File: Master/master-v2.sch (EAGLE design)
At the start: 59 parts, among them J1 ISP, K1 653002114822, K2 653002114822, K3 653002114822, K4 653002114822, U1 ATMEGA128RFA1, U3 ULN2003ANE4, Y1 16MHz, Y2 32.768kHz

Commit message: changes to master-v2
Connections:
- removed net N$21: U$3.SDA
- removed net N$22: U$6.SCL
- removed net N$23: U$6.SDA
- removed net VDD: C12.+, U$2.VO
- net 3.3V: now also C12.+, U$2.VO
- net SCL: now also U$6.SCL
- net SDA: now also U$3.SDA, U$6.SDA
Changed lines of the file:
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@@
 <label x="-5.08" y="99.06" size="1.27" layer="95" rot="MR0" xref="yes"/>
+</segment>
+<segment>
+<pinref part="U$3" gate="G$1" pin="SDA"/>
+<wire x1="-213.36" y1="78.74" x2="-210.82" y2="78.74" width="0.1524" layer="91"/>
+<wire x1="-210.82" y1="78.74" x2="-210.82" y2="81.28" width="0.1524" layer="91"/>
+<wire x1="-210.82" y1="81.28" x2="-208.28" y2="81.28" width="0.1524" layer="91"/>
+<label x="-208.28" y="81.28" size="1.778" layer="95" xref="yes"/>
+</segment>
+<segment>
+<pinref part="U$6" gate="G$1" pin="SDA"/>
+<wire x1="-111.76" y1="78.74" x2="-109.22" y2="78.74" width="0.1524" layer="91"/>
+<wire x1="-109.22" y1="78.74" x2="-109.22" y2="81.28" width="0.1524" layer="91"/>
+<wire x1="-109.22" y1="81.28" x2="-106.68" y2="81.28" width="0.1524" layer="91"/>
+<label x="-106.68" y="81.28" size="1.778" layer="95" xref="yes"/>
 </segment>
 </net>
@@
 <wire x1="-213.36" y1="81.28" x2="-213.36" y2="86.36" width="0.1524" layer="91"/>
 <wire x1="-213.36" y1="86.36" x2="-210.82" y2="86.36" width="0.1524" layer="91"/>
-<label x="-208.28" y="86.36" size="1.778" layer="95"/>
+<label x="-210.82" y="86.36" size="1.778" layer="95" xref="yes"/>
+</segment>
+<segment>
+<pinref part="U$6" gate="G$1" pin="SCL"/>
+<wire x1="-111.76" y1="81.28" x2="-111.76" y2="86.36" width="0.1524" layer="91"/>
+<wire x1="-111.76" y1="86.36" x2="-106.68" y2="86.36" width="0.1524" layer="91"/>
+<label x="-106.68" y="86.36" size="1.778" layer="95" xref="yes"/>
 </segment>
 </net>
@@
 <pinref part="U3" gate="A" pin="4B"/>
 <wire x1="-78.74" y1="226.06" x2="-81.28" y2="226.06" width="0.1524" layer="91"/>
-<label x="-86.36" y="226.06" size="1.778" layer="95"/>
+<label x="-81.28" y="226.06" size="1.778" layer="95" rot="R180" xref="yes"/>
 </segment>
 </net>
@@
 <pinref part="U3" gate="A" pin="3B"/>
 <wire x1="-78.74" y1="228.6" x2="-81.28" y2="228.6" width="0.1524" layer="91"/>
-<label x="-86.36" y="228.6" size="1.778" layer="95"/>
+<label x="-81.28" y="228.6" size="1.778" layer="95" rot="R180" xref="yes"/>
 </segment>
 </net>
@@
 <pinref part="U3" gate="A" pin="2B"/>
 <wire x1="-78.74" y1="231.14" x2="-81.28" y2="231.14" width="0.1524" layer="91"/>
-<label x="-86.36" y="231.14" size="1.778" layer="95"/>
+<label x="-81.28" y="231.14" size="1.778" layer="95" rot="R180" xref="yes"/>
 </segment>
 </net>
@@
 <pinref part="U3" gate="A" pin="1B"/>
 <wire x1="-78.74" y1="233.68" x2="-81.28" y2="233.68" width="0.1524" layer="91"/>
-<label x="-86.36" y="233.68" size="1.778" layer="95"/>
+<label x="-81.28" y="233.68" size="1.778" layer="95" rot="R180" xref="yes"/>
 </segment>
 </net>
@@
 <wire x1="-99.06" y1="76.2" x2="-88.9" y2="76.2" width="0.1524" layer="91"/>
 <junction x="-88.9" y="76.2"/>
+</segment>
+<segment>
+<pinref part="U$2" gate="G$1" pin="VO"/>
+<wire x1="-121.92" y1="172.72" x2="-119.38" y2="172.72" width="0.1524" layer="91"/>
+<pinref part="C12" gate="G$1" pin="+"/>
+<wire x1="-119.38" y1="172.72" x2="-116.84" y2="172.72" width="0.1524" layer="91"/>
+<wire x1="-119.38" y1="167.64" x2="-119.38" y2="172.72" width="0.1524" layer="91"/>
+<junction x="-119.38" y="172.72"/>
+<label x="-116.84" y="172.72" size="1.778" layer="95" xref="yes"/>
 </segment>
 </net>
@@
 </segment>
 </net>
-<net name="VDD" class="0">
-<segment>
-<pinref part="U$2" gate="G$1" pin="VO"/>
-<wire x1="-121.92" y1="172.72" x2="-119.38" y2="172.72" width="0.1524" layer="91"/>
-<label x="-116.84" y="175.26" size="1.778" layer="95"/>
-<pinref part="C12" gate="G$1" pin="+"/>
-<wire x1="-119.38" y1="172.72" x2="-116.84" y2="172.72" width="0.1524" layer="91"/>
-<wire x1="-119.38" y1="167.64" x2="-119.38" y2="172.72" width="0.1524" layer="91"/>
-<junction x="-119.38" y="172.72"/>
-</segment>
-</net>
 <net name="N$1" class="0">
 <segment>
@@
 </segment>
 </net>
-<net name="N$21" class="0">
-<segment>
-<pinref part="U$3" gate="G$1" pin="SDA"/>
-<wire x1="-213.36" y1="78.74" x2="-210.82" y2="78.74" width="0.1524" layer="91"/>
-<wire x1="-210.82" y1="78.74" x2="-210.82" y2="83.82" width="0.1524" layer="91"/>
-<label x="-208.28" y="81.28" size="1.778" layer="95"/>
-</segment>
-</net>
-<net name="N$22" class="0">
-<segment>
-<pinref part="U$6" gate="G$1" pin="SCL"/>
-<wire x1="-111.76" y1="81.28" x2="-111.76" y2="86.36" width="0.1524" layer="91"/>
-<wire x1="-111.76" y1="86.36" x2="-106.68" y2="86.36" width="0.1524" layer="91"/>
-</segment>
-</net>
-<net name="N$23" class="0">
-<segment>
-<pinref part="U$6" gate="G$1" pin="SDA"/>
-<wire x1="-111.76" y1="78.74" x2="-109.22" y2="78.74" width="0.1524" layer="91"/>
-<wire x1="-109.22" y1="78.74" x2="-109.22" y2="83.82" width="0.1524" layer="91"/>
-<wire x1="-109.22" y1="83.82" x2="-106.68" y2="83.82" width="0.1524" layer="91"/>
-</segment>
-</net>

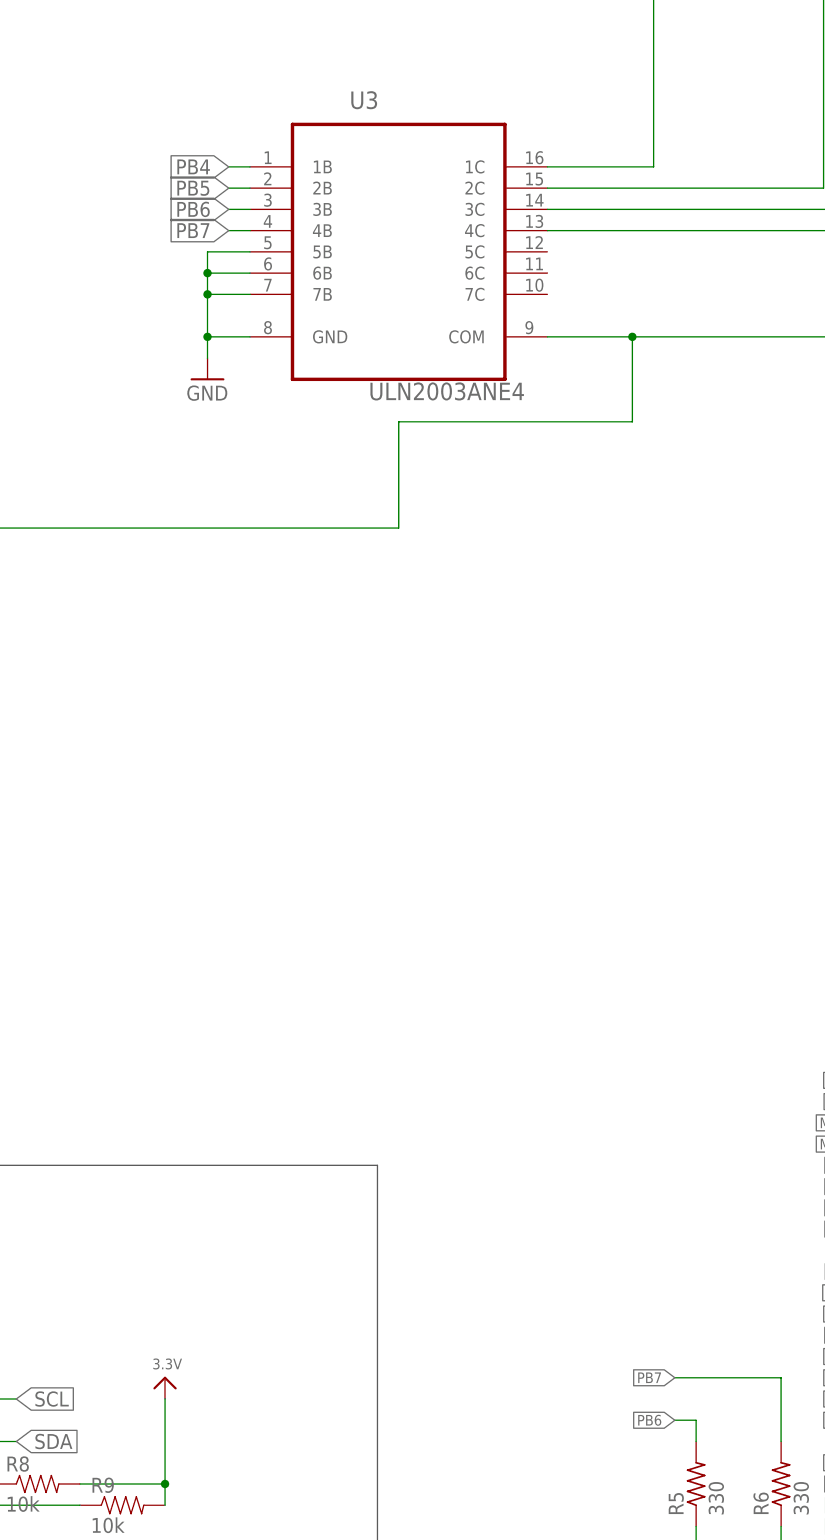
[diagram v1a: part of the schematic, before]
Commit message: Change motor pins in master v2
Changed Pin enumeration for motors. There was one conflict with one Led
so it was changed to another pin. Also routing of those pins was done.
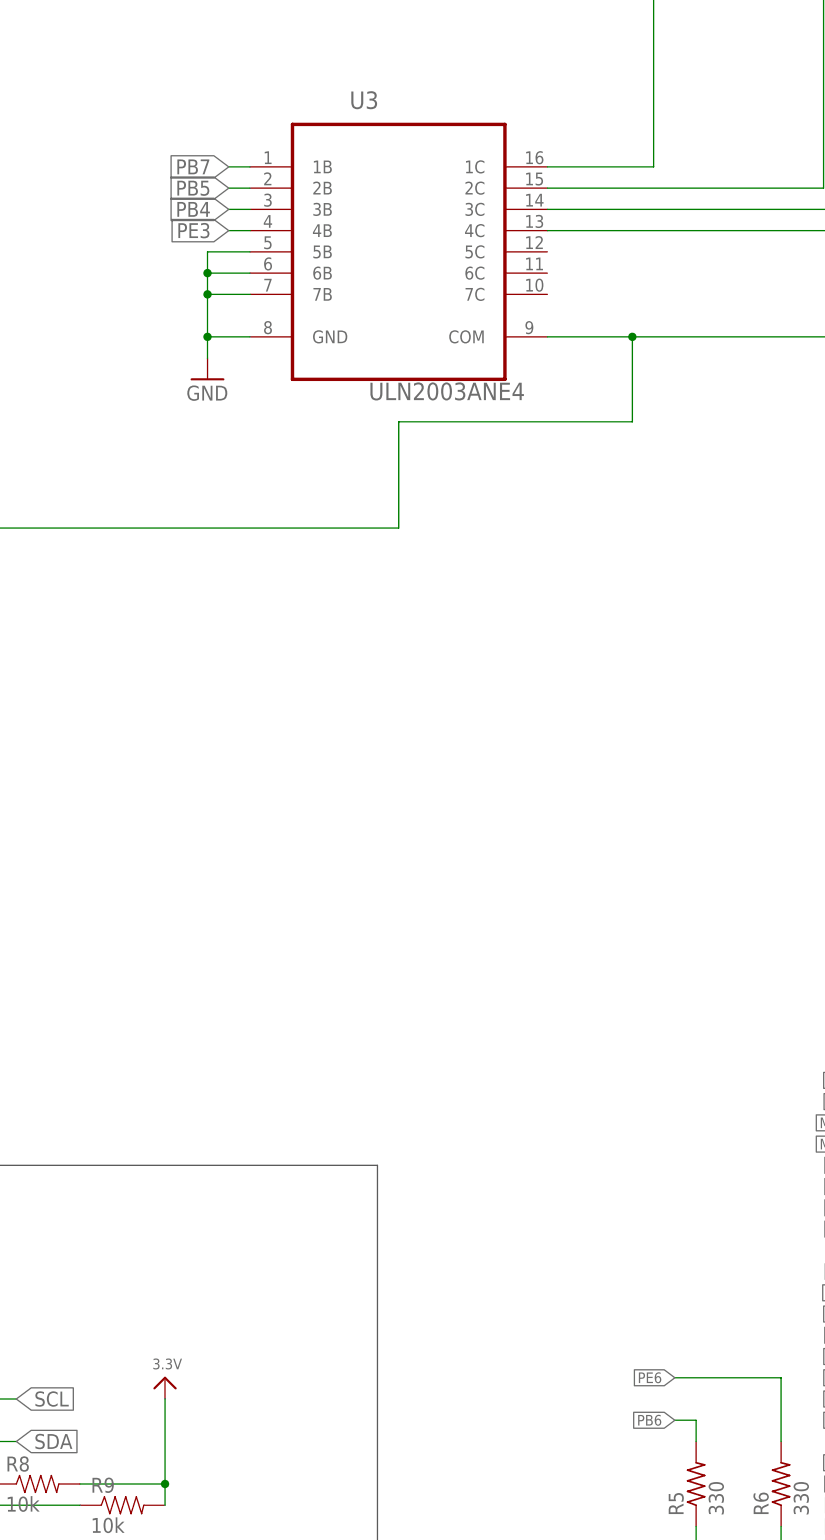
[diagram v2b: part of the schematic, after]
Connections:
- net PB4: now also U3.3B; no longer U3.1B
- net PB6: no longer U3.3B
- net PB7: now also U3.1B; no longer R6.2, U3.4B
- net PE3: now also U3.4B
- net PE6: now also R6.2
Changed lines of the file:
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@@
 <classes>
 <class number="0" name="default" width="0" drill="0">
+<clearance class="0" value="0.205"/>
 </class>
 <class number="1" name="RFSIG" width="0.4572" drill="0">
+<clearance class="0" value="0.205"/>
+<clearance class="1" value="0.205"/>
 </class>
 </classes>
@@
 <label x="-5.08" y="63.5" size="1.27" layer="95" rot="MR0" xref="yes"/>
 </segment>
+<segment>
+<pinref part="R6" gate="G$1" pin="2"/>
+<wire x1="-15.24" y1="81.28" x2="-15.24" y2="88.9" width="0.1524" layer="91"/>
+<wire x1="-15.24" y1="88.9" x2="-27.94" y2="88.9" width="0.1524" layer="91"/>
+<label x="-27.94" y="88.9" size="1.27" layer="95" rot="R180" xref="yes"/>
+</segment>
 </net>
 <net name="PE5" class="0">
@@
 <wire x1="-2.54" y1="71.12" x2="-5.08" y2="71.12" width="0.1524" layer="91"/>
 <label x="-5.08" y="71.12" size="1.27" layer="95" rot="MR0" xref="yes"/>
+</segment>
+<segment>
+<pinref part="U3" gate="A" pin="4B"/>
+<wire x1="-78.74" y1="226.06" x2="-81.28" y2="226.06" width="0.1524" layer="91"/>
+<label x="-81.28" y="226.06" size="1.778" layer="95" rot="R180" xref="yes"/>
 </segment>
 </net>
@@
 </segment>
 <segment>
-<pinref part="R6" gate="G$1" pin="2"/>
-<wire x1="-15.24" y1="81.28" x2="-15.24" y2="88.9" width="0.1524" layer="91"/>
-<wire x1="-15.24" y1="88.9" x2="-27.94" y2="88.9" width="0.1524" layer="91"/>
-<label x="-27.94" y="88.9" size="1.27" layer="95" rot="R180" xref="yes"/>
-</segment>
-<segment>
-<pinref part="U3" gate="A" pin="4B"/>
-<wire x1="-78.74" y1="226.06" x2="-81.28" y2="226.06" width="0.1524" layer="91"/>
-<label x="-81.28" y="226.06" size="1.778" layer="95" rot="R180" xref="yes"/>
+<pinref part="U3" gate="A" pin="1B"/>
+<wire x1="-78.74" y1="233.68" x2="-81.28" y2="233.68" width="0.1524" layer="91"/>
+<label x="-81.28" y="233.68" size="1.778" layer="95" rot="R180" xref="yes"/>
 </segment>
 </net>
@@
 <label x="-27.94" y="83.82" size="1.27" layer="95" rot="R180" xref="yes"/>
 </segment>
+</net>
+<net name="PB5" class="0">
+<segment>
+<pinref part="U1" gate="G$1" pin="PB5(OC1A/PCINT5)"/>
+<label x="-5.08" y="111.76" size="1.27" layer="95" rot="MR0" xref="yes"/>
+<wire x1="-2.54" y1="111.76" x2="-5.08" y2="111.76" width="0.1524" layer="91"/>
+</segment>
+<segment>
+<pinref part="U3" gate="A" pin="2B"/>
+<wire x1="-78.74" y1="231.14" x2="-81.28" y2="231.14" width="0.1524" layer="91"/>
+<label x="-81.28" y="231.14" size="1.778" layer="95" rot="R180" xref="yes"/>
+</segment>
+</net>
+<net name="PB4" class="0">
+<segment>
+<pinref part="U1" gate="G$1" pin="PB4(OC2A/PCINT4)"/>
+<label x="-5.08" y="114.3" size="1.27" layer="95" rot="MR0" xref="yes"/>
+<wire x1="-2.54" y1="114.3" x2="-5.08" y2="114.3" width="0.1524" layer="91"/>
+</segment>
 <segment>
 <pinref part="U3" gate="A" pin="3B"/>
@@
 </segment>
 </net>
-<net name="PB5" class="0">
-<segment>
-<pinref part="U1" gate="G$1" pin="PB5(OC1A/PCINT5)"/>
-<label x="-5.08" y="111.76" size="1.27" layer="95" rot="MR0" xref="yes"/>
-<wire x1="-2.54" y1="111.76" x2="-5.08" y2="111.76" width="0.1524" layer="91"/>
-</segment>
-<segment>
-<pinref part="U3" gate="A" pin="2B"/>
-<wire x1="-78.74" y1="231.14" x2="-81.28" y2="231.14" width="0.1524" layer="91"/>
-<label x="-81.28" y="231.14" size="1.778" layer="95" rot="R180" xref="yes"/>
-</segment>
-</net>
-<net name="PB4" class="0">
-<segment>
-<pinref part="U1" gate="G$1" pin="PB4(OC2A/PCINT4)"/>
-<label x="-5.08" y="114.3" size="1.27" layer="95" rot="MR0" xref="yes"/>
-<wire x1="-2.54" y1="114.3" x2="-5.08" y2="114.3" width="0.1524" layer="91"/>
-</segment>
-<segment>
-<pinref part="U3" gate="A" pin="1B"/>
-<wire x1="-78.74" y1="233.68" x2="-81.28" y2="233.68" width="0.1524" layer="91"/>
-<label x="-81.28" y="233.68" size="1.778" layer="95" rot="R180" xref="yes"/>
-</segment>
-</net>

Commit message: Adding Debug pins
Changed Motor pin numbers and added Debug pins in the schematic.
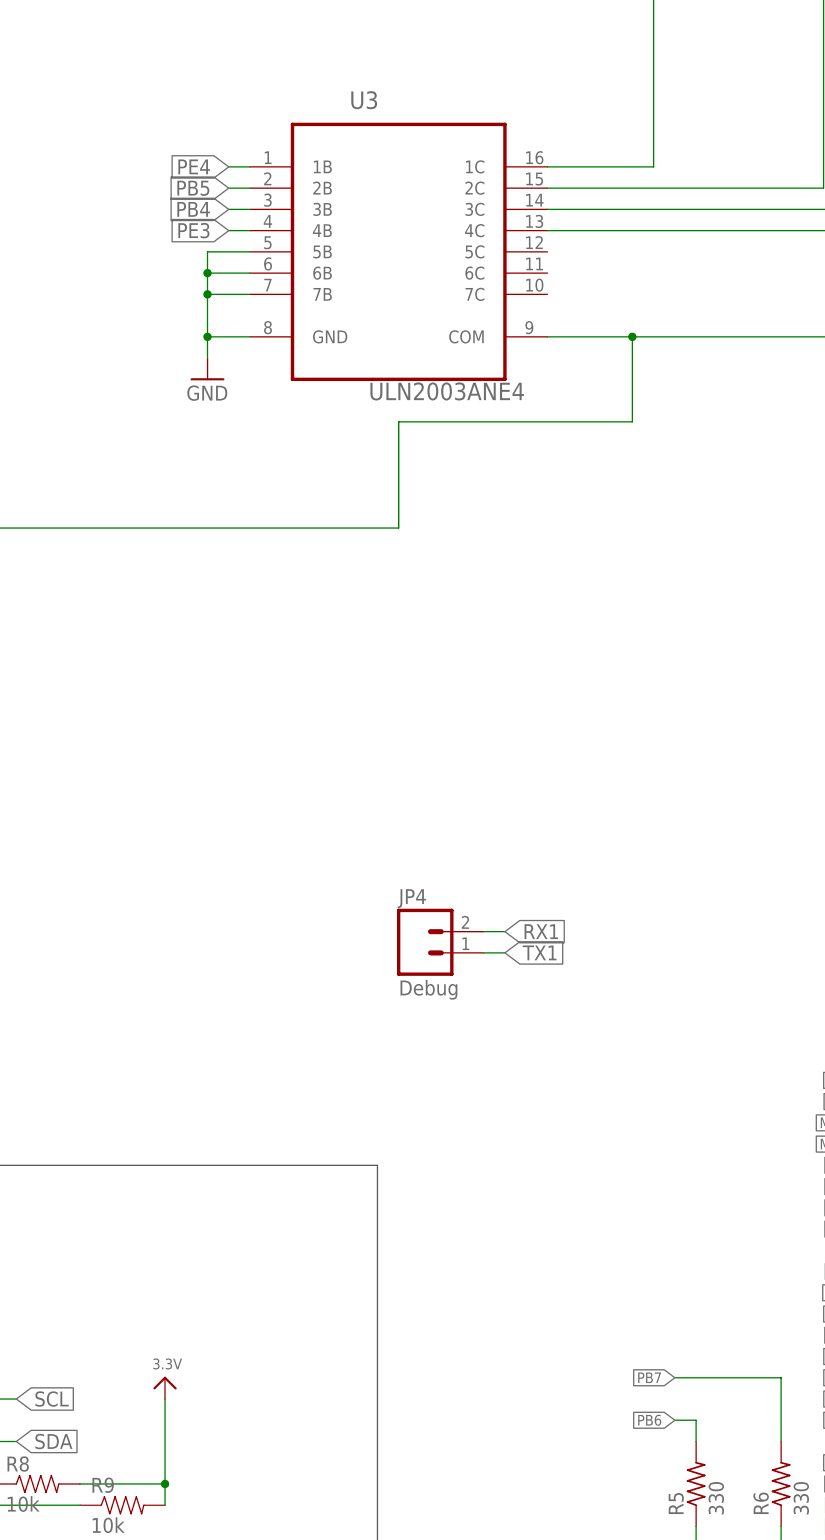
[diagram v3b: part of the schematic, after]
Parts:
- added JP4: Debug, SparkFun:M02PTH
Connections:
- net PB7: now also R6.2; no longer U3.1B
- net PE4: now also U3.1B
- net PE6: no longer R6.2
- net RX1: now also JP4.2
- net TX1: now also JP4.1
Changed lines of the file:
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@@
 </part>
 <part name="GND21" library="supply1" deviceset="GND" device=""/>
+<part name="JP4" library="SparkFun" deviceset="M02" device="PTH" value="Debug"/>
 </parts>
 <sheets>
@@
 </instance>
 <instance part="GND21" gate="1" x="-83.82" y="208.28"/>
+<instance part="JP4" gate="G$1" x="-58.42" y="139.7"/>
 </instances>
 <busses>
@@
 <label x="-5.08" y="63.5" size="1.27" layer="95" rot="MR0" xref="yes"/>
 </segment>
-<segment>
-<pinref part="R6" gate="G$1" pin="2"/>
-<wire x1="-15.24" y1="81.28" x2="-15.24" y2="88.9" width="0.1524" layer="91"/>
-<wire x1="-15.24" y1="88.9" x2="-27.94" y2="88.9" width="0.1524" layer="91"/>
-<label x="-27.94" y="88.9" size="1.27" layer="95" rot="R180" xref="yes"/>
-</segment>
 </net>
 <net name="PE5" class="0">
@@
 <label x="-5.08" y="68.58" size="1.27" layer="95" rot="MR0" xref="yes"/>
 </segment>
+<segment>
+<pinref part="U3" gate="A" pin="1B"/>
+<wire x1="-78.74" y1="233.68" x2="-81.28" y2="233.68" width="0.1524" layer="91"/>
+<label x="-81.28" y="233.68" size="1.778" layer="95" rot="R180" xref="yes"/>
+</segment>
 </net>
 <net name="PE3" class="0">
@@
 <label x="-5.08" y="93.98" size="1.27" layer="95" rot="MR0" xref="yes"/>
 </segment>
+<segment>
+<pinref part="JP4" gate="G$1" pin="1"/>
+<wire x1="-50.8" y1="139.7" x2="-48.26" y2="139.7" width="0.1524" layer="91"/>
+<label x="-48.26" y="139.7" size="1.778" layer="95" xref="yes"/>
+</segment>
 </net>
 <net name="RX1" class="0">
@@
 <wire x1="-2.54" y1="96.52" x2="-5.08" y2="96.52" width="0.1524" layer="91"/>
 <label x="-5.08" y="96.52" size="1.27" layer="95" rot="MR0" xref="yes"/>
+</segment>
+<segment>
+<pinref part="JP4" gate="G$1" pin="2"/>
+<wire x1="-50.8" y1="142.24" x2="-48.26" y2="142.24" width="0.1524" layer="91"/>
+<label x="-48.26" y="142.24" size="1.778" layer="95" xref="yes"/>
 </segment>
 </net>
@@
 </segment>
 <segment>
-<pinref part="U3" gate="A" pin="1B"/>
-<wire x1="-78.74" y1="233.68" x2="-81.28" y2="233.68" width="0.1524" layer="91"/>
-<label x="-81.28" y="233.68" size="1.778" layer="95" rot="R180" xref="yes"/>
-</segment>
-</net>
+<pinref part="R6" gate="G$1" pin="2"/>
+<wire x1="-15.24" y1="81.28" x2="-15.24" y2="88.9" width="0.1524" layer="91"/>
+<wire x1="-15.24" y1="88.9" x2="-27.94" y2="88.9" width="0.1524" layer="91"/>
+<label x="-27.94" y="88.9" size="1.27" layer="95" rot="R180" xref="yes"/>
+</segment>
+</net>
